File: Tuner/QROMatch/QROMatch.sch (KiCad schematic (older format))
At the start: 82 parts, among them J10 Conn_02x12_Odd_Even, J11 Conn_01x01, J12 Conn_01x01, J13 Conn_01x01, J14 Conn_01x01, J2 Conn_01x06

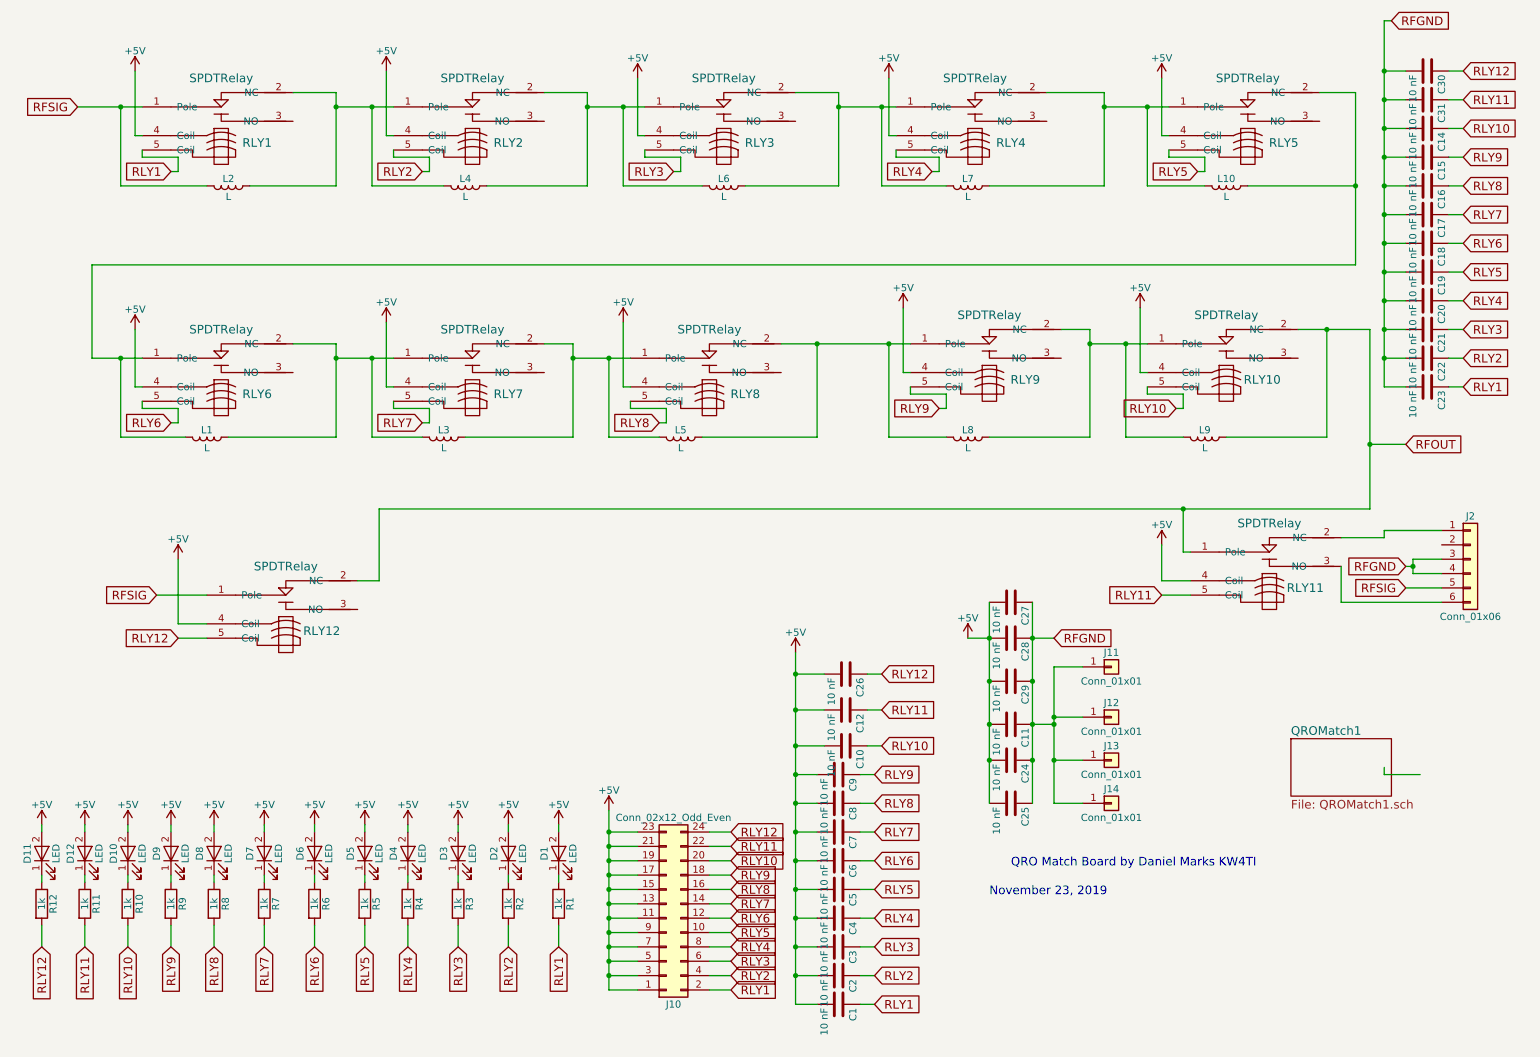
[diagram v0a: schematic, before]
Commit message: Added extra capacitors between relay power and ground posts
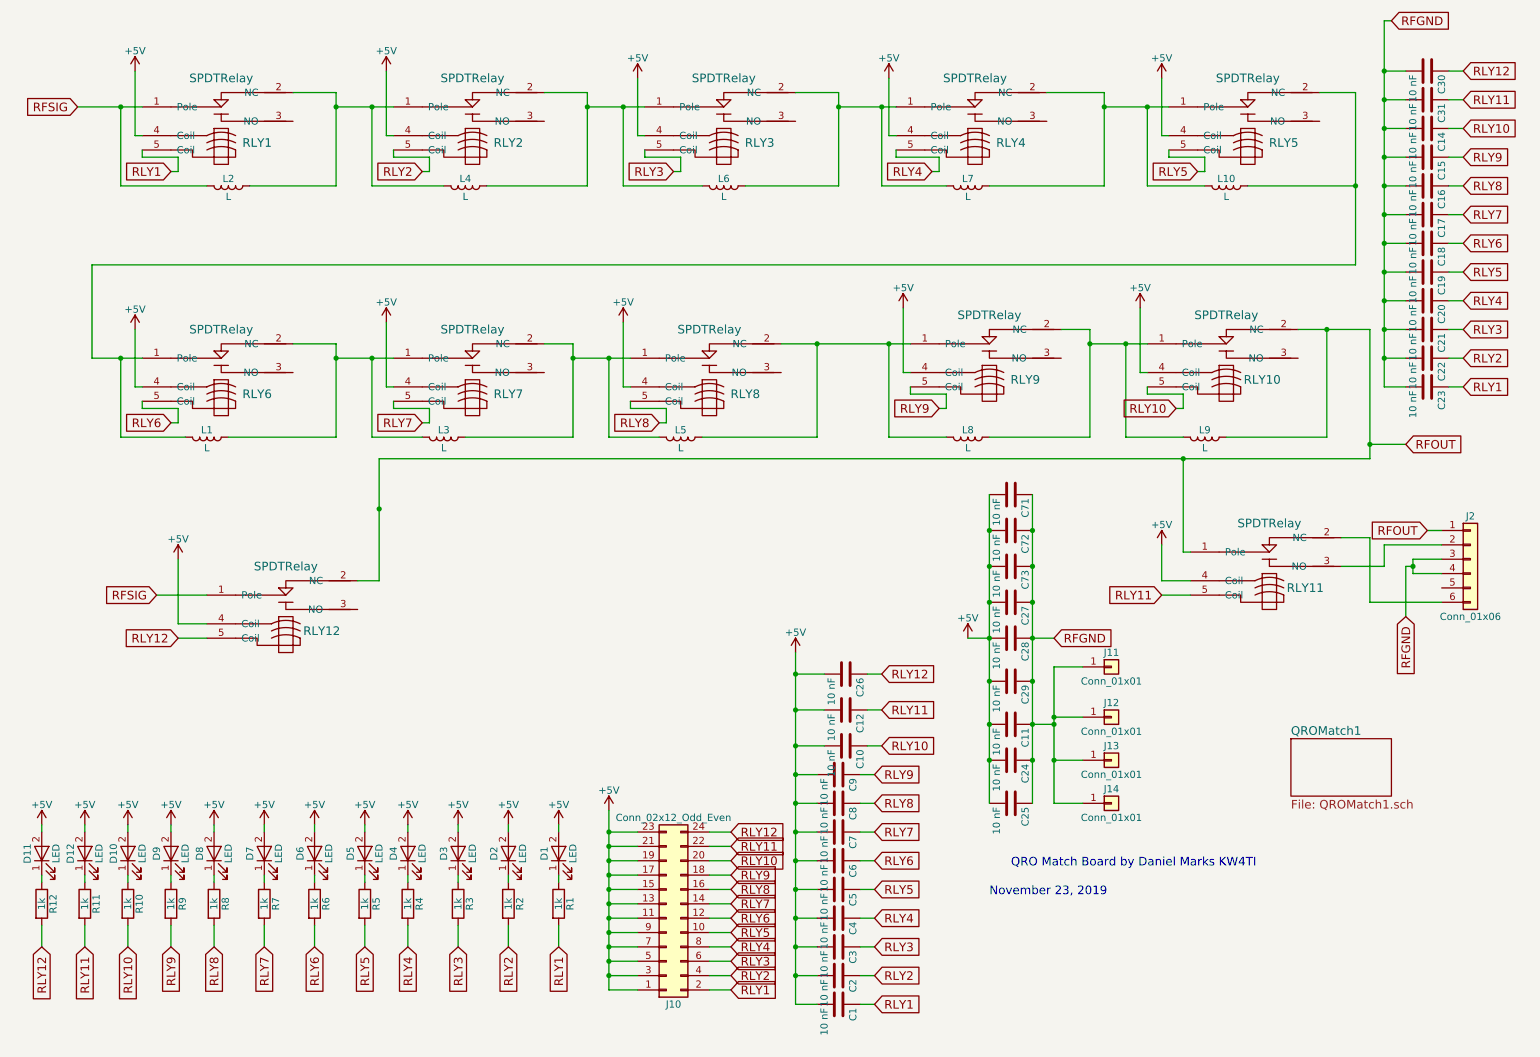
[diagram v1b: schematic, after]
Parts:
- added C71, C72, C73: 10 nF, Capacitors_THT:C_Disc_D5.0mm_W2.5mm_P2.50mm, symbol C
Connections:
- net +5V: now also C71.2, C72.2, C73.2
- net RFGND: now also C71.1, C72.1, C73.1
- net RFOUT: now also J2.1 (Pin_1)
- net RFSIG: no longer J2.5 (Pin_5)
- net at RLY11.2 (NC): now also J2.6 (Pin_6); no longer J2.1 (Pin_1)
- net at RLY11.3 (NO): now also J2.2 (Pin_2); no longer J2.6 (Pin_6)
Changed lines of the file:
@@
 	1    0    0    -1
 $EndComp
-Text GLabel 10250 4600 0    60   Input ~ 0
+Text GLabel 10250 4950 3    60   Input ~ 0
 RFGND
 $Comp
@@
 F1 "QROMatch1.sch" 60
 $EndSheet
-Text GLabel 10250 3750 2    60   Input ~ 0
+Text GLabel 10400 4350 0    60   Input ~ 0
 RFOUT
 $Comp
@@
 	0    1    1    0
 $EndComp
+$Comp
+L C C73
+U 1 1 5DDADA66
+P 7500 4600
+F 0 "C73" H 7525 4700 50  0000 L CNN
+F 1 "10 nF" H 7525 4500 50  0000 L CNN
+F 2 "Capacitors_THT:C_Disc_D5.0mm_W2.5mm_P2.50mm" H 7538 4450 50  0001 C CNN
+F 3 "" H 7500 4600 50  0001 C CNN
+	1    7500 4600
+	0    1    1    0
+$EndComp
+$Comp
+L C C72
+U 1 1 5DDADB75
+P 7500 4350
+F 0 "C72" H 7525 4450 50  0000 L CNN
+F 1 "10 nF" H 7525 4250 50  0000 L CNN
+F 2 "Capacitors_THT:C_Disc_D5.0mm_W2.5mm_P2.50mm" H 7538 4200 50  0001 C CNN
+F 3 "" H 7500 4350 50  0001 C CNN
+	1    7500 4350
+	0    1    1    0
+$EndComp
+$Comp
+L C C71
+U 1 1 5DDAF043
+P 7500 4100
+F 0 "C71" H 7525 4200 50  0000 L CNN
+F 1 "10 nF" H 7525 4000 50  0000 L CNN
+F 2 "Capacitors_THT:C_Disc_D5.0mm_W2.5mm_P2.50mm" H 7538 3950 50  0001 C CNN
+F 3 "" H 7500 4100 50  0001 C CNN
+	1    7500 4100
+	0    1    1    0
+$EndComp
 Wire Wire Line
 	8750 4800 8550 4800
-Connection ~ 8700 4200
-Wire Wire Line
-	8700 4500 8700 4200
-Wire Wire Line
-	8750 4500 8700 4500
-Wire Wire Line
-	10000 4200 3100 4200
-Wire Wire Line
-	3100 4200 3100 4700
+Wire Wire Line
+	8700 3850 8700 4500
+Wire Wire Line
+	8700 4500 8750 4500
+Wire Wire Line
+	3100 3850 3100 4700
 Wire Wire Line
 	9900 1300 9900 2500
@@
 	9500 2950 10000 2950
 Wire Wire Line
-	10000 2950 10000 4200
+	10000 2950 10000 3850
 Wire Wire Line
 	3100 4700 2950 4700
@@
 	10100 800  10150 800
 Wire Wire Line
-	7650 4850 7650 6250
+	7650 4100 7650 6250
 Connection ~ 7650 5100
 Connection ~ 7650 5400
@@
 Connection ~ 7650 5950
 Wire Wire Line
-	7350 4850 7350 6250
+	7350 4100 7350 6250
 Connection ~ 7350 5950
 Connection ~ 7350 5700
@@
 	7800 5100 7650 5100
 Wire Wire Line
-	9800 4400 10100 4400
-Wire Wire Line
-	10100 4400 10100 4350
-Wire Wire Line
-	10100 4350 10500 4350
-Wire Wire Line
-	9800 4600 9800 4850
-Wire Wire Line
-	9800 4850 10500 4850
-Wire Wire Line
 	8550 4450 8550 4700
 Wire Wire Line
@@
 Wire Wire Line
 	1100 2500 1100 3150
-Text GLabel 10250 4750 0    60   Input ~ 0
-RFSIG
-Wire Wire Line
-	10250 4750 10500 4750
-Wire Wire Line
-	10350 6050 10100 6050
-Wire Wire Line
-	10100 6050 10100 6000
+Connection ~ 7650 4850
+Connection ~ 7650 4600
+Connection ~ 7350 4850
+Connection ~ 7350 4600
+Wire Wire Line
+	10000 3850 3100 3850
+Connection ~ 3100 4200
+Connection ~ 8700 3850
+Connection ~ 7650 4350
+Connection ~ 7350 4350
+Wire Wire Line
+	10000 4850 10500 4850
+Wire Wire Line
+	10400 4350 10500 4350
+Wire Wire Line
+	10000 4850 10000 4400
+Wire Wire Line
+	10000 4400 9800 4400
+Wire Wire Line
+	10250 4600 10250 4950
+Wire Wire Line
+	10500 4450 10100 4450
+Wire Wire Line
+	10100 4450 10100 4600
+Wire Wire Line
+	10100 4600 9800 4600
+Text GLabel 10250 3750 2    60   Input ~ 0
+RFOUT
 $EndSCHEMATC

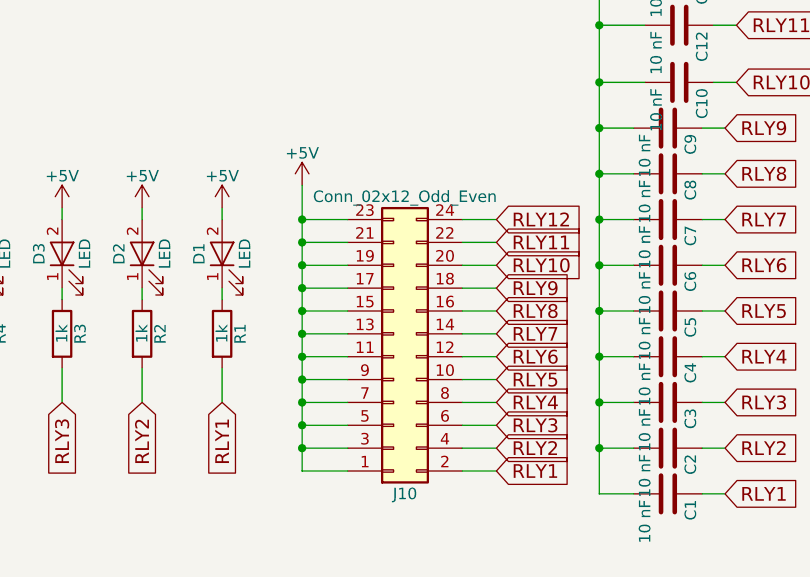
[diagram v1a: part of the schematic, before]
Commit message: Changed from 2x12 IDC to more common 2x13 IDC
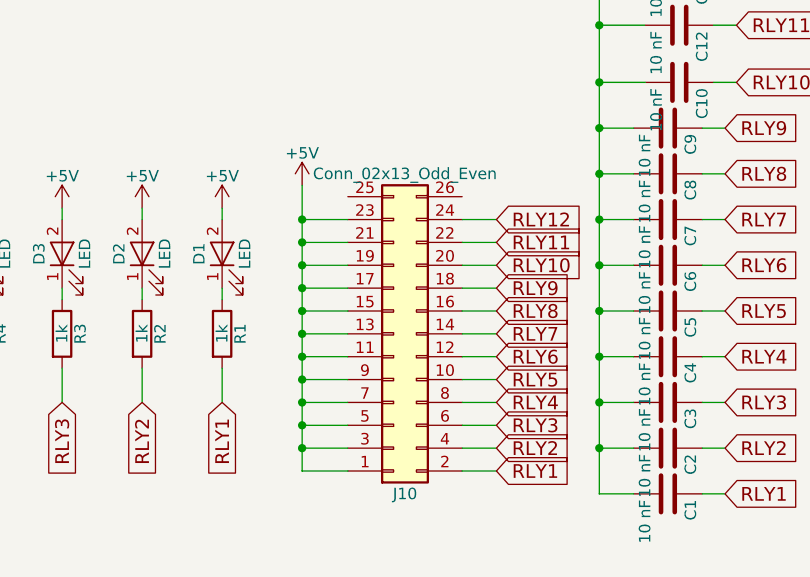
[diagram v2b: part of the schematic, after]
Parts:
- removed J10: Conn_02x12_Odd_Even, Pin_Headers:Pin_Header_Straight_2x12_Pitch2.54mm, symbol Conn_02x12_Odd_Even
- added J10: Conn_02x13_Odd_Even, Pin_Headers:Pin_Header_Straight_2x13_Pitch2.54mm, symbol Conn_02x13_Odd_Even
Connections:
- net +5V: now also J10.1 (Pin_1), J10.11 (Pin_11), J10.13 (Pin_13), J10.15 (Pin_15), J10.17 (Pin_17), J10.19 (Pin_19), J10.21 (Pin_21), J10.23 (Pin_23), J10.3 (Pin_3), J10.5 (Pin_5), J10.7 (Pin_7), J10.9 (Pin_9)
- net RLY1: now also J10.2 (Pin_2)
- net RLY10: now also J10.20 (Pin_20)
- net RLY11: now also J10.22 (Pin_22)
- net RLY12: now also J10.24 (Pin_24)
- net RLY2: now also J10.4 (Pin_4)
- net RLY3: now also J10.6 (Pin_6)
- net RLY4: now also J10.8 (Pin_8)
- net RLY5: now also J10.10 (Pin_10)
- net RLY6: now also J10.12 (Pin_12)
- net RLY7: now also J10.14 (Pin_14)
- net RLY8: now also J10.16 (Pin_16)
- net RLY9: now also J10.18 (Pin_18)
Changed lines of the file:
@@
 Text GLabel 8550 4800 0    60   Input ~ 0
 RLY11
-$Comp
-L Conn_02x12_Odd_Even J10
-U 1 1 5DDAAF51
-P 5100 7050
-F 0 "J10" H 5150 7650 50  0000 C CNN
-F 1 "Conn_02x12_Odd_Even" H 5150 6350 50  0000 C CNN
-F 2 "Pin_Headers:Pin_Header_Straight_2x12_Pitch2.54mm" H 5100 7050 50  0001 C CNN
-F 3 "" H 5100 7050 50  0001 C CNN
-	1    5100 7050
-	1    0    0    1
-$EndComp
 Text GLabel 5550 6550 2    60   Input ~ 0
 RLY11
@@
 Text GLabel 10250 3750 2    60   Input ~ 0
 RFOUT
+$Comp
+L Conn_02x13_Odd_Even J10
+U 1 1 5DE1E298
+P 5100 6950
+F 0 "J10" H 5150 7650 50  0000 C CNN
+F 1 "Conn_02x13_Odd_Even" H 5150 6250 50  0000 C CNN
+F 2 "Pin_Headers:Pin_Header_Straight_2x13_Pitch2.54mm" H 5100 6950 50  0001 C CNN
+F 3 "" H 5100 6950 50  0001 C CNN
+	1    5100 6950
+	1    0    0    1
+$EndComp
 $EndSCHEMATC
